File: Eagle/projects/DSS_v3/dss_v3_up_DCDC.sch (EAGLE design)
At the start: 56 parts, among them IC1 MC34063AD, IC2 Atmega8a, IC3 TL431, J1 12-24V, SW1 EC12E_SW, T1 BC846, X1 PS2

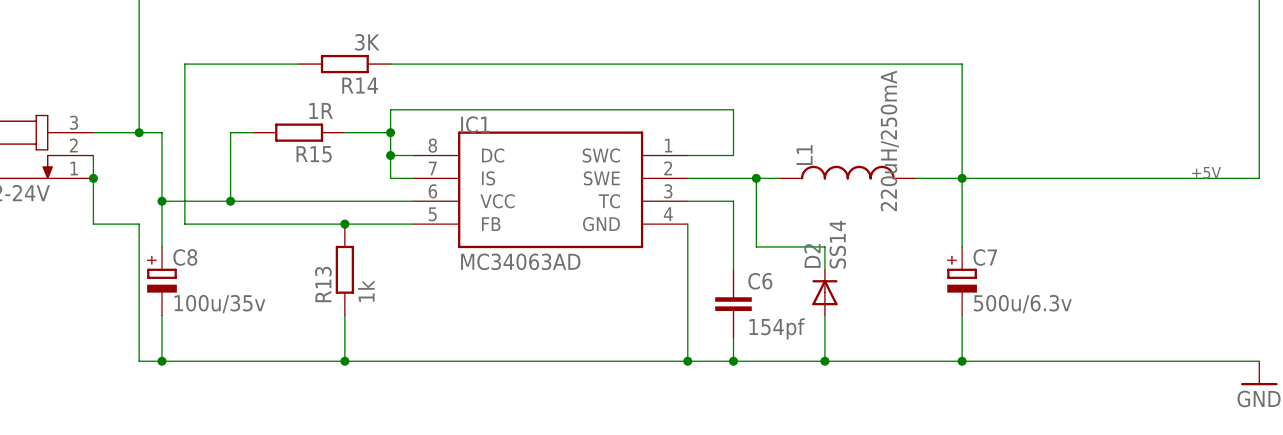
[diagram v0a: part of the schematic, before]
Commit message: gnd fix add smd capacitor for select
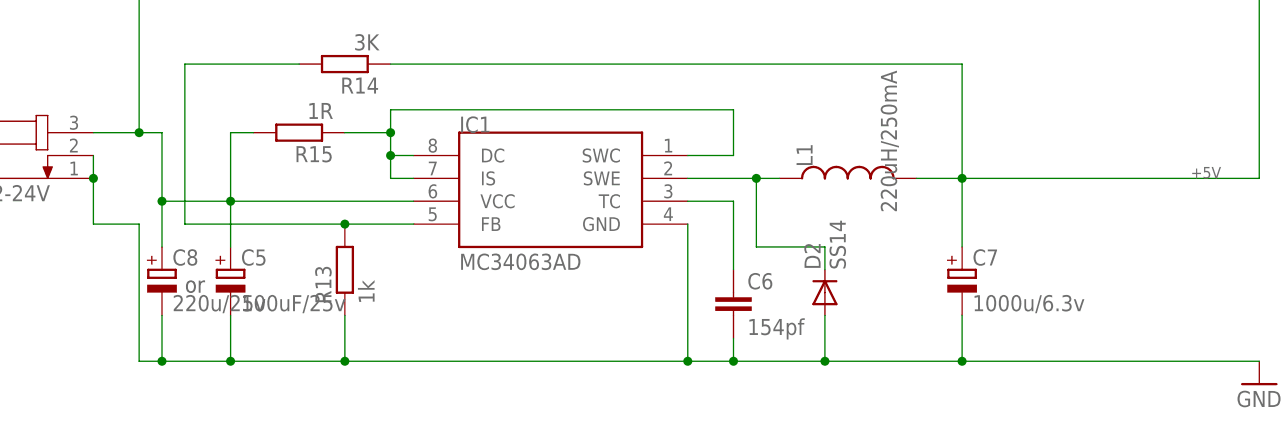
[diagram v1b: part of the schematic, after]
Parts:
- added C5: 100uF/25v, rcl:CPOL-EUCT7343
- C7: value 500u/6.3v -> 1000u/6.3v
- C8: value 100u/35v -> 220u/25v
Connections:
- net GND: now also C5.-
- net HTR+: now also C5.+
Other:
- note added: "or"

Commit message: update
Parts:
- C5: device rcl:CPOL-EUCT7343 -> rcl:CPOL-EUCT6032
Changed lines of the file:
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@@
 <part name="LED2" library="led" library_urn="urn:adsk.eagle:library:259" deviceset="LED" device="CHIP-LED0805" package3d_urn="urn:adsk.eagle:package:15818/2" value="RED"/>
 <part name="LED3" library="led" library_urn="urn:adsk.eagle:library:259" deviceset="LED" device="CHIP-LED0805" package3d_urn="urn:adsk.eagle:package:15818/2" value="GREEN"/>
-<part name="C5" library="rcl" library_urn="urn:adsk.eagle:library:334" deviceset="CPOL-EU" device="CT7343" package3d_urn="urn:adsk.eagle:package:23304/2" value="100uF/25v"/>
+<part name="C5" library="rcl" library_urn="urn:adsk.eagle:library:334" deviceset="CPOL-EU" device="CT6032" package3d_urn="urn:adsk.eagle:package:23305/2" value="100uF/25v"/>
 </parts>
 <sheets>

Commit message: update
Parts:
- removed LED3: GREEN, led:LEDCHIP-LED0805
- added LED1: RED, led:LEDCHIP-LED0805
- LED2: value RED -> GREEN
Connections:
- net GND: now also LED1.C; no longer LED3.C
- net N$15: now also LED2.A; no longer LED3.A
- net N$2: now also LED1.A; no longer LED2.A
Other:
- moved on the sheet: LED2
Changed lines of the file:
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@@
 <part name="D1" library="diode" deviceset="DIODE-" device="DO214AC" value="SS14"/>
 <part name="T1" library="transistor-neu-to92" deviceset="BC846" device=""/>
-<part name="C1" library="rcl" deviceset="C-EU" device="C0805" value="100nF"/>
+<part name="C1" library="rcl" library_urn="urn:adsk.eagle:library:334" deviceset="C-EU" device="C0805" package3d_urn="urn:adsk.eagle:package:23617/2" value="100nF"/>
 <part name="R1" library="rcl" library_urn="urn:adsk.eagle:library:334" deviceset="R-EU_" device="R0805" package3d_urn="urn:adsk.eagle:package:23553/2" value="470R"/>
 <part name="R2" library="rcl" deviceset="R-EU_" device="R0805" value="10K"/>
@@
 <part name="R22" library="rcl" library_urn="urn:adsk.eagle:library:334" deviceset="R-EU_" device="R0805" package3d_urn="urn:adsk.eagle:package:23553/2" value="510R"/>
 <part name="R23" library="rcl" library_urn="urn:adsk.eagle:library:334" deviceset="R-EU_" device="R0805" package3d_urn="urn:adsk.eagle:package:23553/2" value="510R"/>
-<part name="C11" library="rcl" deviceset="C-EU" device="C0805" value="100nf"/>
+<part name="C11" library="rcl" library_urn="urn:adsk.eagle:library:334" deviceset="C-EU" device="C0805" package3d_urn="urn:adsk.eagle:package:23617/2" value="100nf"/>
 <part name="GND5" library="supply1" deviceset="GND" device=""/>
-<part name="C12" library="rcl" deviceset="C-EU" device="C0805" value="100nf"/>
+<part name="C12" library="rcl" library_urn="urn:adsk.eagle:library:334" deviceset="C-EU" device="C0805" package3d_urn="urn:adsk.eagle:package:23617/2" value="100nf"/>
 <part name="C13" library="rcl" deviceset="C-EU" device="C0805" value="100nf"/>
 <part name="R24" library="rcl" deviceset="R-EU_" device="R0805" value="360R"/>
@@
 <part name="GND9" library="supply1" deviceset="GND" device=""/>
 <part name="SW1" library="switch-alps" deviceset="EC12E_SW" device=""/>
-<part name="LED2" library="led" library_urn="urn:adsk.eagle:library:259" deviceset="LED" device="CHIP-LED0805" package3d_urn="urn:adsk.eagle:package:15818/2" value="RED"/>
-<part name="LED3" library="led" library_urn="urn:adsk.eagle:library:259" deviceset="LED" device="CHIP-LED0805" package3d_urn="urn:adsk.eagle:package:15818/2" value="GREEN"/>
+<part name="LED1" library="led" library_urn="urn:adsk.eagle:library:259" deviceset="LED" device="CHIP-LED0805" package3d_urn="urn:adsk.eagle:package:15818/2" value="RED"/>
+<part name="LED2" library="led" library_urn="urn:adsk.eagle:library:259" deviceset="LED" device="CHIP-LED0805" package3d_urn="urn:adsk.eagle:package:15818/2" value="GREEN"/>
 <part name="C5" library="rcl" library_urn="urn:adsk.eagle:library:334" deviceset="CPOL-EU" device="CT6032" package3d_urn="urn:adsk.eagle:package:23305/2" value="100uF/25v"/>
 </parts>
@@
 <attribute name="VALUE" x="223.52" y="20.32" size="1.27" layer="96" rot="R270"/>
 </instance>
-<instance part="LED2" gate="G$1" x="226.06" y="58.42" smashed="yes">
+<instance part="LED1" gate="G$1" x="226.06" y="58.42" smashed="yes">
 <attribute name="NAME" x="232.156" y="53.848" size="1.778" layer="95" rot="R90"/>
 <attribute name="VALUE" x="234.315" y="53.848" size="1.778" layer="96" rot="R90"/>
 </instance>
-<instance part="LED3" gate="G$1" x="226.06" y="45.72" smashed="yes" rot="R180">
+<instance part="LED2" gate="G$1" x="226.06" y="45.72" smashed="yes" rot="R180">
 <attribute name="NAME" x="230.124" y="50.292" size="1.778" layer="95" rot="R270"/>
 <attribute name="VALUE" x="233.045" y="50.292" size="1.778" layer="96" rot="R270"/>
@@
 <pinref part="GND7" gate="1" pin="GND"/>
 <wire x1="215.9" y1="53.34" x2="226.06" y2="53.34" width="0.1524" layer="91"/>
+<pinref part="LED1" gate="G$1" pin="C"/>
 <pinref part="LED2" gate="G$1" pin="C"/>
-<pinref part="LED3" gate="G$1" pin="C"/>
 <wire x1="226.06" y1="53.34" x2="226.06" y2="50.8" width="0.1524" layer="91"/>
 <junction x="226.06" y="53.34"/>
@@
 <pinref part="R25" gate="G$1" pin="1"/>
 <wire x1="223.52" y1="63.5" x2="226.06" y2="63.5" width="0.1524" layer="91"/>
+<pinref part="LED1" gate="G$1" pin="A"/>
+<wire x1="226.06" y1="63.5" x2="226.06" y2="60.96" width="0.1524" layer="91"/>
+</segment>
+</net>
+<net name="N$15" class="0">
+<segment>
+<pinref part="R26" gate="G$1" pin="1"/>
 <pinref part="LED2" gate="G$1" pin="A"/>
-<wire x1="226.06" y1="63.5" x2="226.06" y2="60.96" width="0.1524" layer="91"/>
-</segment>
-</net>
-<net name="N$15" class="0">
-<segment>
-<pinref part="R26" gate="G$1" pin="1"/>
-<pinref part="LED3" gate="G$1" pin="A"/>
 <wire x1="223.52" y1="43.18" x2="226.06" y2="43.18" width="0.1524" layer="91"/>
 </segment>

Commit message: update
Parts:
- SW1: device switch-alps:EC12E_SW -> switch-alps_3D:EC12E_SW

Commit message: update
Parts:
- added ON-OFF_HEAT: (no value), jumper:JP1Q
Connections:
- new net N$17: ON-OFF_HEAT.2, R4.1
- net SH: now also ON-OFF_HEAT.1; no longer R4.1
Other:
- note added: "отключение нагрева жала для калибровки температуры резистором R7"
- note removed: "отключение нагрева жала"
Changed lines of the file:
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@@
 <setting verticaltext="up"/>
 </settings>
-<grid distance="0.1" unitdist="inch" unit="inch" style="lines" multiple="1" display="no" altdistance="0.01" altunitdist="inch" altunit="inch"/>
+<grid distance="0.1" unitdist="inch" unit="inch" style="lines" multiple="1" display="yes" altdistance="0.01" altunitdist="inch" altunit="inch"/>
 <layers>
 <layer number="1" name="Top" color="4" fill="1" visible="no" active="no"/>
@@
 <part name="LED2" library="led" library_urn="urn:adsk.eagle:library:259" deviceset="LED" device="CHIP-LED0805" package3d_urn="urn:adsk.eagle:package:15818/2" value="GREEN"/>
 <part name="C5" library="rcl" library_urn="urn:adsk.eagle:library:334" deviceset="CPOL-EU" device="CT6032" package3d_urn="urn:adsk.eagle:package:23305/2" value="100uF/25v"/>
+<part name="ON-OFF_HEAT" library="jumper" library_urn="urn:adsk.eagle:library:252" deviceset="JP1Q" device="" package3d_urn="urn:adsk.eagle:package:15455/1"/>
 </parts>
 <sheets>
@@
 <text x="8.636" y="41.656" size="1.778" layer="91">+5V</text>
 <text x="-33.02" y="43.18" size="1.778" layer="91">+24v</text>
-<text x="13.97" y="23.876" size="1.778" layer="97">отключение нагрева жала</text>
+<text x="13.97" y="23.876" size="0.8128" layer="97">отключение нагрева жала для калибровки температуры резистором R7</text>
 <text x="214.122" y="10.668" size="1.27" layer="91">c</text>
 <text x="209.296" y="18.288" size="1.27" layer="91">a</text>
@@
 <attribute name="NAME" x="-95.377" y="-40.1574" size="1.778" layer="95"/>
 <attribute name="VALUE" x="-95.377" y="-45.2374" size="1.778" layer="96"/>
+</instance>
+<instance part="ON-OFF_HEAT" gate="A" x="33.02" y="30.48" smashed="yes" rot="R90">
+<attribute name="NAME" x="38.1" y="27.94" size="1.778" layer="95" rot="R180"/>
+<attribute name="VALUE" x="38.1" y="34.925" size="1.778" layer="96" rot="R180"/>
 </instance>
 </instances>
@@
 <net name="SH" class="0">
 <segment>
-<label x="56.642" y="23.368" size="1.778" layer="95"/>
-<wire x1="5.08" y1="22.86" x2="60.96" y2="22.86" width="0.1524" layer="91"/>
-<pinref part="R4" gate="G$1" pin="1"/>
-</segment>
-<segment>
 <pinref part="IC2" gate="1" pin="PB1(OC1A)"/>
 <wire x1="193.04" y1="20.32" x2="200.66" y2="20.32" width="0.1524" layer="91"/>
 <label x="195.58" y="20.32" size="1.27" layer="95"/>
+</segment>
+<segment>
+<wire x1="60.96" y1="22.86" x2="40.64" y2="22.86" width="0.1524" layer="91"/>
+<pinref part="ON-OFF_HEAT" gate="A" pin="1"/>
+<wire x1="40.64" y1="30.48" x2="40.64" y2="22.86" width="0.1524" layer="91"/>
 </segment>
 </net>
@@
 </segment>
 </net>
+<net name="N$17" class="0">
+<segment>
+<pinref part="R4" gate="G$1" pin="1"/>
+<wire x1="5.08" y1="22.86" x2="25.4" y2="22.86" width="0.1524" layer="91"/>
+<pinref part="ON-OFF_HEAT" gate="A" pin="2"/>
+<wire x1="25.4" y1="30.48" x2="25.4" y2="22.86" width="0.1524" layer="91"/>
+</segment>
+</net>

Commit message: update
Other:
- note added: "R7 подбор 40-63 Ом равно сопротивлению т.резистора паяльника при комнатной t=22С минус 3-5 Ом Базовая калибровка: При снаятом джампере отображаемая температура жала должна соответсвовать комнотной."
- note removed: "R7 подбор 40-63 Ом равно сопротивлению т.резистора паяльника при комнатной t=22С минус 3-5 Ом"
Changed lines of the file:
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@@
 <setting verticaltext="up"/>
 </settings>
-<grid distance="0.1" unitdist="inch" unit="inch" style="lines" multiple="1" display="yes" altdistance="0.01" altunitdist="inch" altunit="inch"/>
+<grid distance="0.1" unitdist="inch" unit="inch" style="lines" multiple="1" display="no" altdistance="0.01" altunitdist="inch" altunit="inch"/>
 <layers>
 <layer number="1" name="Top" color="4" fill="1" visible="no" active="no"/>
@@
 <sheet>
 <plain>
-<text x="-15.24" y="60.96" size="1.27" layer="97">R7 подбор 40-63 Ом
+<text x="25.4" y="35.56" size="1.27" layer="97">R7 подбор 40-63 Ом
 равно сопротивлению
 т.резистора паяльника
 при комнатной t=22С
-минус 3-5 Ом</text>
+минус 3-5 Ом
+Базовая калибровка:
+При снаятом джампере отображаемая
+температура жала должна
+соответсвовать комнотной.</text>
 <text x="8.636" y="41.656" size="1.778" layer="91">+5V</text>
 <text x="-33.02" y="43.18" size="1.778" layer="91">+24v</text>
@@
 <text x="-14.478" y="14.224" size="1.778" layer="97">R4 Зависит от операционного
              усилителя</text>
-<text x="-101.6" y="-43.18" size="1.778" layer="97">or</text>
+<text x="-101.346" y="-42.418" size="1.778" layer="97">or</text>
 </plain>
 <instances>
@@
 <instance part="C8" gate="G$1" x="-104.14" y="-40.64" smashed="yes">
 <attribute name="NAME" x="-102.997" y="-40.1574" size="1.778" layer="95"/>
-<attribute name="VALUE" x="-102.997" y="-45.2374" size="1.778" layer="96"/>
+<attribute name="VALUE" x="-108.077" y="-45.2374" size="1.778" layer="96"/>
 </instance>
 <instance part="D2" gate="G$1" x="-30.48" y="-43.18" smashed="yes" rot="R90">
@@
 <instance part="C5" gate="G$1" x="-96.52" y="-40.64" smashed="yes">
 <attribute name="NAME" x="-95.377" y="-40.1574" size="1.778" layer="95"/>
-<attribute name="VALUE" x="-95.377" y="-45.2374" size="1.778" layer="96"/>
+<attribute name="VALUE" x="-97.917" y="-47.7774" size="1.778" layer="96"/>
 </instance>
 <instance part="ON-OFF_HEAT" gate="A" x="33.02" y="30.48" smashed="yes" rot="R90">
